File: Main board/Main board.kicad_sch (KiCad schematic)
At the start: 102 parts, among them CN1 PA001-4P, CN2 PA001-4P, J1 TagConnect_TC2030-NL, J2 Conn_01x02_Pin, J3 Conn_01x02_Pin, J5 Connector, USB-TYPE-C-16P, J6 436500201, J7 Conn_01x04_Pin, J8 Conn_01x04_Pin, Q1 SI7232DN-T1-GE3, Q2 SI7232DN-T1-GE3, Q3 SI7232DN-T1-GE3, SW1 SKRKAEE020, SW2 SKRKAEE020, U1 STM32U575VGTx, U10 TLV75733PDBV, U11 NRVB120VLSFT1G, U12 NRVB120VLSFT1G, U2 TPS62901RPJR, U7 SN74AHCT125DR, X1 1XXD32000MBA, Y1 ECS-327TXO-33-TR

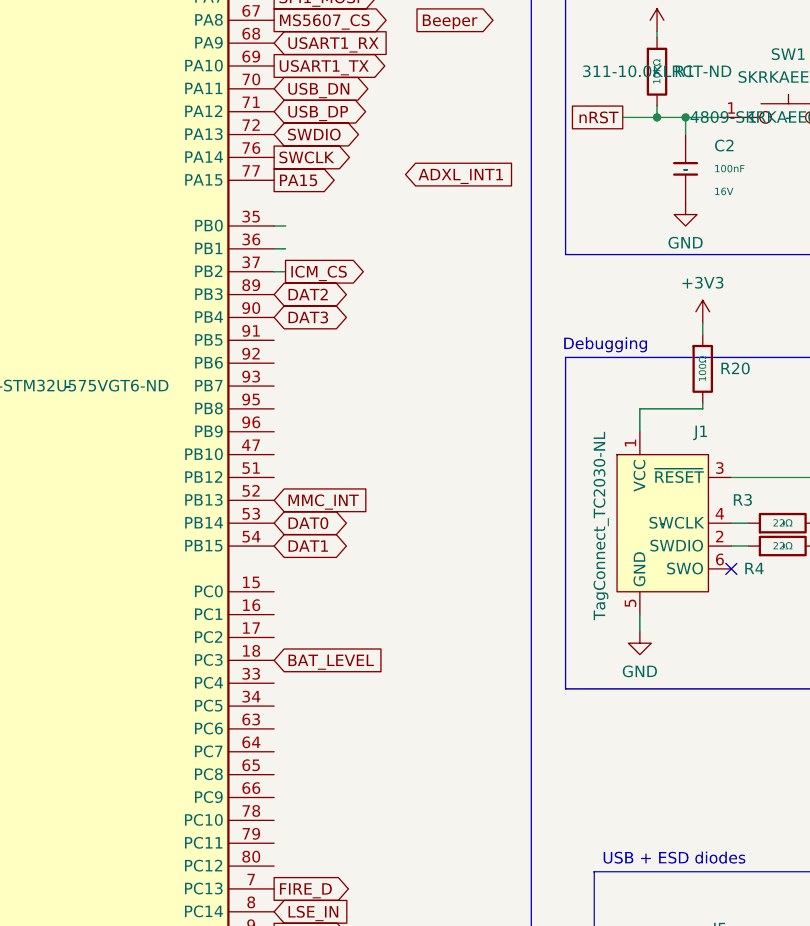
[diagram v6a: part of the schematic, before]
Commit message: Minor Adjustment + Silkscreen
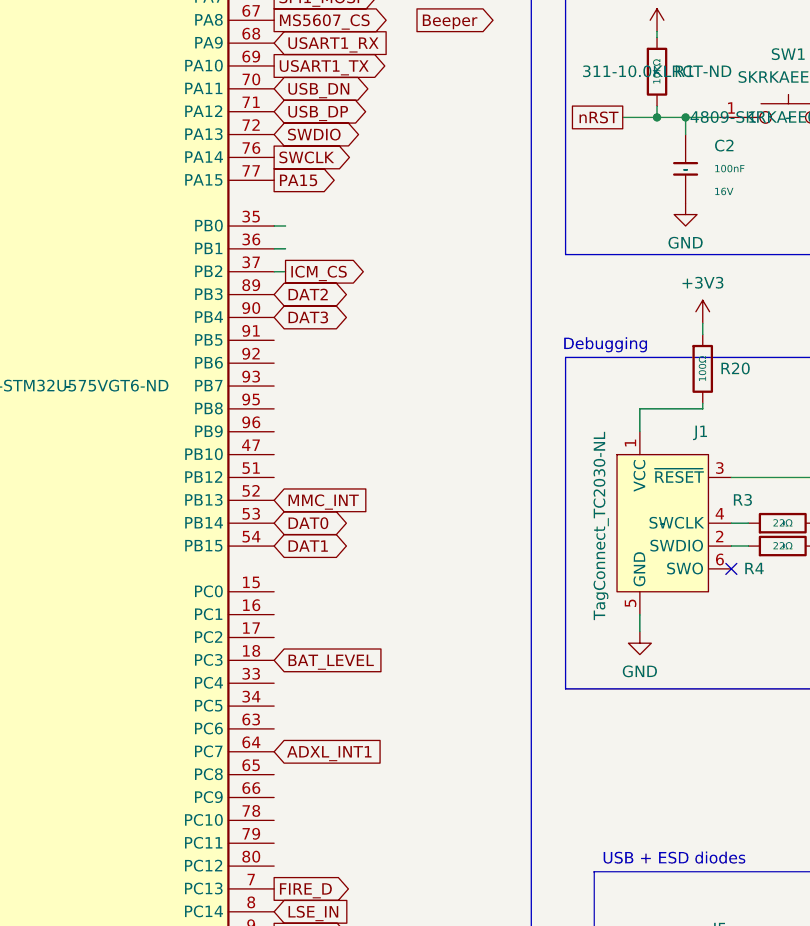
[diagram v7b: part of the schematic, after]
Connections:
- net ADXL_INT1: now also U1.64 (PC7)
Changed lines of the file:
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@@
 	(global_label "ADXL_INT1"
 		(shape input)
-		(at 93.345 86.995 0)
+		(at 78.74 151.13 0)
 		(fields_autoplaced yes)
 		(effects
@@
 		)
 		(property "Intersheetrefs" "${INTERSHEET_REFS}"
-			(at 106.0064 86.995 0)
+			(at 91.4014 151.13 0)
 			(effects
 				(font

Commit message: Included IMU project
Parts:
- removed BUZZER1: PS1440P02BT, EASYEDA:BUZ-TH_BD14.0-P5.00-D0.7-FD, symbol EasyEDA:PS1440P02BT
- removed C33: 100nF, PCM_JLCPCB:C_0402, symbol PCM_JLCPCB-Capacitors:0402,100nF
- removed Q3: SI7232DN-T1-GE3, EASYEDA:POWER-1212-8_L3.3-W3.3-P0.66-LS3.3-BL, symbol EasyEDA:SI7232DN-T1-GE3
- removed R29: 47kΩ, PCM_JLCPCB:R_0402, symbol PCM_JLCPCB-Resistors:0402,47kΩ
- removed R30: 1kΩ, PCM_JLCPCB:R_0402, symbol PCM_JLCPCB-Resistors:0402,1kΩ
- added D6: Yellow, LEDDD:WL-SMCW_0603, symbol Device:LED
- added D7: GREEN, LEDDD:WL-SMCW_0603, symbol Device:LED
- added R29, R44: 470Ω, PCM_JLCPCB:R_0402, symbol PCM_JLCPCB-Resistors:0402,470Ω
- J6: footprint molex1x03:CONN_SD-43650-001_02_MOL -> Connector_AMASS:AMASS_XT30UPB-F_1x02_P5.0mm_Vertical
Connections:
- net +3V3: now also R20.2, R29.2; no longer R20.1
- net GND: now also D6.1 (K), D7.1 (K)
- net ICM_INT_1: now also U1.35 (PB0)
- net at J1.1 (VCC): now also R20.1; no longer R20.2
- net PB6: now reaches U1.92 (PB6)
- net PB6: now also R44.2
- new net: D7.2 (A), R29.1
- new net: D6.2 (A), R44.1
- no-connect marks 12 -> 51
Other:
- note added: "Pyrotechnique channels"
- note removed: "Beeper"
- note removed: "Pyro"
- company: (none) -> Chulalongkorn University High Altitude Research (CUHAR)
- title: (none) -> CURFA-V SRAD Flight Computer
- moved on the sheet: C1, C10, C11, C12, C13, C14, C15, C2, C25, C26, C27, C28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
